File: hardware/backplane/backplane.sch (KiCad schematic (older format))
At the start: 12 parts, among them J1 C96ABC, J2 C96ABC, J3 C96ABC, J4 C96ABC, J5 C96ABC, J6 C96ABC, J7 C96ABC, J8 C96ABC

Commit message: start to put clock hardware on the backplane
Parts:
- added C1, C2: 0.01μF, Capacitor_THT:C_Rect_L7.0mm_W3.5mm_P5.00mm, symbol Device:C
- added C3, C4: 1μF, Capacitor_THT:C_Rect_L7.0mm_W3.5mm_P5.00mm, symbol Device:C
- added CB1, CB2, CB3, CB4, CB5, CB6: 0.1μF, Capacitor_THT:C_Rect_L7.0mm_W3.5mm_P5.00mm, symbol Device:C_Small
- added CBU1, CBU2, CBU3, CBU4, CBX1: 0.1μF, Capacitor_THT:C_Rect_L7.0mm_W3.5mm_P5.00mm, symbol Device:C
- added CR1, CR2: 1μF, Capacitor_THT:C_Rect_L7.0mm_W3.5mm_P5.00mm, symbol Device:C_Small
- added D1, D2: DIODE, Diode_THT:D_DO-15_P2.54mm_Vertical_AnodeUp, symbol pspice:DIODE
- added J9: C96ABC, Connector_DIN:DIN41612_C_3x32_Female_Vertical_THT, symbol Connector:C96ABC
- added JP1: Jumper_NO_Small, Connector_PinHeader_2.54mm:PinHeader_1x02_P2.54mm_Vertical, symbol Device:Jumper_NO_Small
- added JPC1: JP_RST, Connector_PinHeader_2.54mm:PinHeader_1x02_P2.54mm_Vertical, symbol Jumper:Jumper_2_Open
- added R1, R9: 4.7k, Resistor_THT:R_Axial_DIN0207_L6.3mm_D2.5mm_P2.54mm_Vertical, symbol Device:R
- added R10, R11, R4, R6, R7, R8: 1k, Resistor_THT:R_Axial_DIN0207_L6.3mm_D2.5mm_P2.54mm_Vertical, symbol Device:R
- added R2: 1M, Resistor_THT:R_Axial_DIN0207_L6.3mm_D2.5mm_P2.54mm_Vertical, symbol Device:R
- added R3: 100k, Resistor_THT:R_Axial_DIN0207_L6.3mm_D2.5mm_P2.54mm_Vertical, symbol Device:R
- added R5: 100k, Connector_PinHeader_2.54mm:PinHeader_1x02_P2.54mm_Vertical, symbol Device:R_Variable
- added SW1: SW_Push, Connector_PinHeader_2.54mm:PinHeader_1x02_P2.54mm_Vertical, symbol Switch:SW_Push
- added SW2, SW3: SW_SPDT, Connector_PinHeader_2.54mm:PinHeader_1x03_P2.54mm_Vertical, symbol Switch:SW_SPDT
- added U1: 74AHC14, Package_DIP:DIP-14_W7.62mm_Socket, symbol 74xx:74LS14
- added U10: U13, Package_DIP:DIP-14_W7.62mm_Socket, symbol 74xx:74HC00
- added U2, U3: 74AHC08, Package_DIP:DIP-14_W7.62mm_Socket, symbol 74xx:74LS08
- added U4: 74HC00, Package_DIP:DIP-14_W7.62mm_Socket, symbol 74xx:74HC00
- added U5, U6: 74AHC74, Package_DIP:DIP-14_W7.62mm_Socket, symbol 74xx:74LS74
- added U7: NE556, Package_DIP:DIP-14_W7.62mm_Socket, symbol Timer:NE556
- added U8: 74AHC32, Package_DIP:DIP-14_W7.62mm_Socket, symbol 74xx:74LS32
- added U9: 74AHCT125, Package_DIP:DIP-14_W7.62mm_Socket, symbol 74xx:74LS125
- added X1: CXO_DIP8, Package_DIP:DIP-8_W7.62mm_Socket, symbol Oscillator:CXO_DIP8
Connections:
- net A10: now also J9.A10 (10A)
- net A11: now also J9.A11 (11A)
- net A12: now also J9.A12 (12A)
- net A13: now also J9.A13 (13A)
- net A14: now also J9.A14 (14A)
- net A15: now also J9.A15 (15A)
- net A16: now also J9.A16 (16A)
- net A17: now also J9.A17 (17A)
- net A18: now also J9.A18 (18A)
- net A19: now also J9.A19 (19A)
- net A2: now also J9.A2 (2A)
- net A20: now also J9.A20 (20A)
- net A21: now also J9.A21 (21A)
- net A22: now also J9.A22 (22A)
- net A23: now also J9.A23 (23A)
- net A24: now also J9.A24 (24A)
- net A25: now also J9.A25 (25A)
- net A26: now also J9.A26 (26A)
- net A27: now also J9.A27 (27A), U2.4
- net A28: now also J9.A28 (28A), U8.8
- net A29: now also J9.A29 (29A)
- net A3: now also J9.A3 (3A)
- net A30: now also J9.A30 (30A)
- net A31: now also J9.A31 (31A), U1.1, U2.9, U6.11 (C)
- net A4: now also J9.A4 (4A)
- net A5: now also J9.A5 (5A)
- net A6: now also J9.A6 (6A)
- net A7: now also J9.A7 (7A)
- net A8: now also J9.A8 (8A)
- net A9: now also J9.A9 (9A)
- net C10: now also J9.C10 (10C)
- net C11: now also J9.C11 (11C)
- net C12: now also J9.C12 (12C)
- net C13: now also J9.C13 (13C)
- net C14: now also J9.C14 (14C)
- net C15: now also J9.C15 (15C)
- net C16: now also J9.C16 (16C)
- net C17: now also J9.C17 (17C)
- net C18: now also J9.C18 (18C)
- net C19: now also J9.C19 (19C)
- net C2: now also J9.C2 (2C)
- net C20: now also J9.C20 (20C)
- net C21: now also J9.C21 (21C)
- net C22: now also J9.C22 (22C)
- net C23: now also J9.C23 (23C), U1.8
- net C24: now also J9.C24 (24C)
- net C25: now also J9.C25 (25C)
- net C26: now also J9.C26 (26C)
- net C27: now also J9.C27 (27C)
- net C28: now also J9.C28 (28C)
- net C29: now also J9.C29 (29C)
- net C3: now also J9.C3 (3C)
- net C30: now also J9.C30 (30C)
- net C31: now also D1.2 (A), D2.2 (A), J9.C31 (31C), JPC1.1 (A), R1.2
- net C4: now also J9.C4 (4C)
- net C5: now also J9.C5 (5C)
- net C6: now also J9.C6 (6C)
- net C7: now also J9.C7 (7C)
- net C8: now also J9.C8 (8C)
- net C9: now also J9.C9 (9C)
- net GND: now also C1.2, C2.2, C3.2, C4.2, CB1.2, CB2.2, CB3.2, CB4.2, CB5.2, CB6.1, CBU1.2, CBU2.2, CBU3.2, CBU4.2, CBX1.2, CR1.2, CR2.2, J9.A32 (32A), J9.B32 (32B), J9.C32 (32C), JP1.1, JPC1.2 (B), SW1.1, SW3.2 (B), U1.7 (GND), U10.7 (GND), U2.7 (GND), U3.10, U3.12, U3.13, U3.4, U3.5, U3.7 (GND), U3.9, U4.7 (GND), U5.7 (GND), U6.7 (GND), U7.7 (GND), U7.7 (GND), U8.7 (GND), U9.7 (GND), X1.4 (GND)
- net VCC: now also CB1.1, CB2.1, CB3.1, CB4.1, CB5.1, CB6.2, CBU1.1, CBU2.1, CBU3.1, CBU4.1, CBX1.1, J9.A1 (1A), J9.B1 (1B), J9.C1 (1C), R1.1, R10.1, R11.1, R2.1, R3.1, R4.1, R7.1, R8.1, R9.1, U1.14 (VCC), U10.14 (VCC), U2.14 (VCC), U3.14 (VCC), U4.14 (VCC), U5.14 (VCC), U6.14 (VCC), U7.10 (R), U7.14 (VCC), U7.14 (VCC), U7.4 (R), U8.14 (VCC), U9.14 (VCC), X1.8 (Vcc)
- new net: U1.2, U5.3 (C)
- new net: U1.4, U6.3 (C)
- new net: U1.11, U1.12
- new net: U2.11, U8.10
- new net: U2.8, U8.9
- new net: U3.1, U9.11
- new net: SW2.2 (B), U9.12
- new net: U2.3, U5.2 (D)
- new net: U5.5 (Q), U6.12 (D)
- new net: U2.6, U6.2 (D)
- new net: U5.12 (D), U6.5 (Q)
- new net: U2.2, U5.8 (~Q)
- new net: U2.12, U5.9 (Q)
- new net: U2.5, U6.8 (~Q)
- new net: U2.10, U6.9 (Q)
- new net: CR1.1, D1.1 (K), R2.2, U1.5
- new net: R5.1, R6.1
- new net: R6.2, R7.2, U7.1 (DIS)
- new net: C3.1, R5.2, U7.2 (THR), U7.6 (TR)
- new net: C1.1, U7.3 (CV)
- new net: CR2.1, D2.1 (K), R3.2, U1.13
- new net: C4.1, R8.2, U7.12 (THR), U7.13 (DIS)
- new net: R4.2, SW1.2, U7.8 (TR)
- new net: C2.1, U7.11 (CV)
- new net: R11.2, SW3.1 (A), U10.1
- new net: R10.2, SW3.3 (C), U10.5
- new net: U4.10, U4.6
- new net: U4.3, U4.9
- new net +5V: U5.10 (~S), U5.4 (~S), U6.10 (~S), U6.4 (~S)
- new net 555_AST: U4.2, U7.5 (Q)
- new net 555_CLK: SW2.3 (C), U4.8
- new net 555_MONO: U4.5, U7.9 (Q)
- new net BASE_CLK: U3.3
- new net BUS_ACTIVE: U2.1
- new net RST-unused: U1.6, U1.9
- new net SEL_AST: U10.3, U10.4, U4.1
- new net SEL_MONO: U10.2, U10.6, U4.4
- new net SYS_CLK: U1.3, U2.13, U5.11 (C)
- new net XO: SW2.1 (A), X1.5 (OUT)
- new net ~CLK_ENABLE~: JP1.2, R9.2, U9.13
- new net ~CLK_RST~: U1.10, U3.2, U5.1 (~R), U5.13 (~R), U6.1 (~R), U6.13 (~R)
- no-connect marks 30 -> 66
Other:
- note added: "Clock switcher"
- note added: "Reset signals"
- note added: "shorter clock rst pulse s.t. \nclock starts before other ICs"
- moved on the sheet: H1, H2, H3, H4, J1, J2, J3, J4, J5, J6, J7, J8

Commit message: backplane: shrink by 1mm in both dimensions and start rearranging components
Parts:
- H4: footprint rails:SHF8-R -> rails:SHF8-L
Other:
- moved on the sheet: H1, H2, H3, H4
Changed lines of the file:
@@
 L Mechanical:MountingHole H4
 U 1 1 6046743B
-P -850 -7950
-F 0 "H4" H -750 -7904 50  0000 L CNN
-F 1 "MountingHole" H -750 -7995 50  0000 L CNN
-F 2 "rails:SHF8-R" H -850 -7950 50  0001 C CNN
-F 3 "~" H -850 -7950 50  0001 C CNN
-	1    -850 -7950
+P -2500 8100
+F 0 "H4" H -2400 8146 50  0000 L CNN
+F 1 "MountingHole" H -2400 8055 50  0000 L CNN
+F 2 "rails:SHF8-L" H -2500 8100 50  0001 C CNN
+F 3 "~" H -2500 8100 50  0001 C CNN
+	1    -2500 8100
 	1    0    0    -1
 $EndComp
@@
 L Mechanical:MountingHole H3
 U 1 1 604683EA
-P -950 -8550
-F 0 "H3" H -850 -8504 50  0000 L CNN
-F 1 "MountingHole" H -850 -8595 50  0000 L CNN
-F 2 "rails:SHF8-L" H -950 -8550 50  0001 C CNN
-F 3 "~" H -950 -8550 50  0001 C CNN
-	1    -950 -8550
+P -2600 7500
+F 0 "H3" H -2500 7546 50  0000 L CNN
+F 1 "MountingHole" H -2500 7455 50  0000 L CNN
+F 2 "rails:SHF8-L" H -2600 7500 50  0001 C CNN
+F 3 "~" H -2600 7500 50  0001 C CNN
+	1    -2600 7500
 	1    0    0    -1
 $EndComp
@@
 L Mechanical:MountingHole H2
 U 1 1 60468515
-P -1050 -9000
-F 0 "H2" H -950 -8954 50  0000 L CNN
-F 1 "MountingHole" H -950 -9045 50  0000 L CNN
-F 2 "rails:SHF8-R" H -1050 -9000 50  0001 C CNN
-F 3 "~" H -1050 -9000 50  0001 C CNN
-	1    -1050 -9000
+P -2700 7050
+F 0 "H2" H -2600 7096 50  0000 L CNN
+F 1 "MountingHole" H -2600 7005 50  0000 L CNN
+F 2 "rails:SHF8-R" H -2700 7050 50  0001 C CNN
+F 3 "~" H -2700 7050 50  0001 C CNN
+	1    -2700 7050
 	1    0    0    -1
 $EndComp
@@
 L Mechanical:MountingHole H1
 U 1 1 604686C3
-P -1050 -9550
-F 0 "H1" H -950 -9504 50  0000 L CNN
-F 1 "MountingHole" H -950 -9595 50  0000 L CNN
-F 2 "rails:SHF8-L" H -1050 -9550 50  0001 C CNN
-F 3 "~" H -1050 -9550 50  0001 C CNN
-	1    -1050 -9550
+P -2700 6500
+F 0 "H1" H -2600 6546 50  0000 L CNN
+F 1 "MountingHole" H -2600 6455 50  0000 L CNN
+F 2 "rails:SHF8-L" H -2700 6500 50  0001 C CNN
+F 3 "~" H -2700 6500 50  0001 C CNN
+	1    -2700 6500
 	1    0    0    -1
 $EndComp

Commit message: backplane: remove the base/bus clock switch
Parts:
- removed CB1, CB3, CB4, CB5, CB6: 0.1μF, Capacitor_THT:C_Rect_L7.0mm_W3.5mm_P5.00mm, symbol Device:C_Small
- removed U3: 74AHC08, Package_DIP:DIP-14_W7.62mm_Socket, symbol 74xx:74LS08
- removed U5, U6: 74AHC74, Package_DIP:DIP-14_W7.62mm_Socket, symbol 74xx:74LS74
- removed U8: 74AHC32, Package_DIP:DIP-14_W7.62mm_Socket, symbol 74xx:74LS32
- added J10: Conn_Coaxial_Power, Connector_Phoenix_MSTB:PhoenixContact_MSTBVA_2,5_2-G-5,08_1x02_P5.08mm_Vertical, symbol Connector:Conn_Coaxial_Power
- added TP1, TP10, TP11, TP12, TP13, TP14, TP15, TP16, TP17, TP18, TP19, TP2, TP20, TP21, TP22, TP23, TP24, TP25, TP26, TP27, TP28, TP29, TP3, TP30, TP4, TP5, TP6, TP7, TP8, TP9: TestPoint, TestPoint:TestPoint_THTPad_D1.0mm_Drill0.5mm, symbol Connector:TestPoint
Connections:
- net BUS_ACTIVE is gone; now on net GND: U2.1
- net A27: no longer U2.4
- net A28: now also U2.11
- net A31: no longer U1.1, U2.9
- net B10J1: now also TP9.1
- net B11J1: now also TP10.1
- net B12J1: now also TP11.1
- net B13J1: now also TP12.1
- net B14J1: now also TP13.1
- net B15J1: now also TP14.1
- net B16J1: now also TP15.1
- net B17J1: now also TP16.1
- net B18J1: now also TP17.1
- net B19J1: now also TP18.1
- net B20J1: now also TP19.1
- net B21J1: now also TP20.1
- net B22J1: now also TP21.1
- net B23J1: now also TP22.1
- net B24J1: now also TP23.1
- net B25J1: now also TP24.1
- net B26J1: now also TP25.1
- net B27J1: now also TP26.1
- net B28J1: now also TP27.1
- net B29J1: now also TP28.1
- net B2J1: now also TP1.1
- net B30J1: now also TP29.1
- net B31J1: now also TP30.1
- net B3J1: now also TP2.1
- net B4J1: now also TP3.1
- net B5J1: now also TP4.1
- net B6J1: now also TP5.1
- net B7J1: now also TP6.1
- net B8J1: now also TP7.1
- net B9J1: now also TP8.1
- net C31: no longer D1.2 (A), D2.2 (A), JPC1.1 (A), R1.2
- net GND: now also U1.1, U1.3, U10.10, U10.12, U10.13, U10.9, U2.10, U2.2, U2.4, U2.5, U2.9, U4.12, U4.13, U9.2, U9.5, U9.9, J10.2 (Ext)
- net VCC: now also U9.1, U9.10, U9.4, J10.1 (In)
- net ~CLK_RST~: now also U2.13
- net CLK_RST: now reaches U1.11, U1.12
- net at U9.11: now also U2.12
- net RST-unused: no longer names the net of U1.6, U1.9
- removed net SYS_CLK: U1.3, U2.13
- new net ~RST_HDR~: D1.2 (A), D2.2 (A), JPC1.1 (A), R1.2
- no-connect marks 66 -> 72
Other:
- note removed: "Clock switcher"
- moved on the sheet: C1, C2, C3, C4, CB2, CBU1, CBU2, CBU3, CBU4, CBX1, CR1, CR2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

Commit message: backplane: bump some clearance hole diameters
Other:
- moved on the sheet: C1, C2, C3, C4, CR1, CR2, D1, D2, H1, H2, H3, H4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

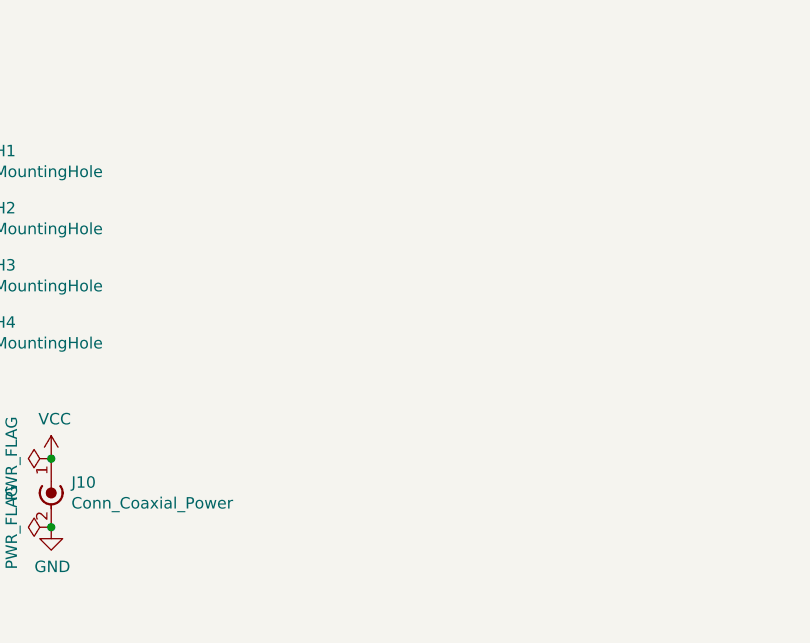
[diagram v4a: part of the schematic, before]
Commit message: backplane: use less mounting hardware
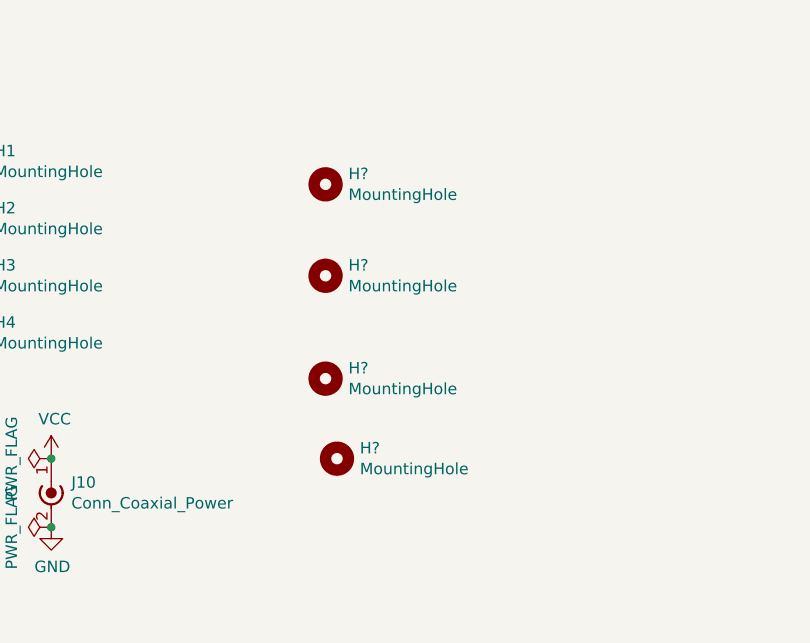
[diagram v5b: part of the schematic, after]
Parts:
- added H? (x4): MountingHole, rails:7mm, symbol Mechanical:MountingHole
- H1, H3, H4: footprint rails:SHF8-L -> rails:8mm
- H2: footprint rails:SHF8-R -> rails:8mm
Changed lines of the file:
@@
 F 0 "H4" H 12250 5546 50  0000 L CNN
 F 1 "MountingHole" H 12250 5455 50  0000 L CNN
-F 2 "rails:SHF8-L" H 12150 5500 50  0001 C CNN
+F 2 "rails:8mm" H 12150 5500 50  0001 C CNN
 F 3 "~" H 12150 5500 50  0001 C CNN
 	1    12150 5500
@@
 F 0 "H3" H 12250 5296 50  0000 L CNN
 F 1 "MountingHole" H 12250 5205 50  0000 L CNN
-F 2 "rails:SHF8-L" H 12150 5250 50  0001 C CNN
+F 2 "rails:8mm" H 12150 5250 50  0001 C CNN
 F 3 "~" H 12150 5250 50  0001 C CNN
 	1    12150 5250
@@
 F 0 "H2" H 12250 5046 50  0000 L CNN
 F 1 "MountingHole" H 12250 4955 50  0000 L CNN
-F 2 "rails:SHF8-R" H 12150 5000 50  0001 C CNN
+F 2 "rails:8mm" H 12150 5000 50  0001 C CNN
 F 3 "~" H 12150 5000 50  0001 C CNN
 	1    12150 5000
@@
 F 0 "H1" H 12250 4796 50  0000 L CNN
 F 1 "MountingHole" H 12250 4705 50  0000 L CNN
-F 2 "rails:SHF8-L" H 12150 4750 50  0001 C CNN
+F 2 "rails:8mm" H 12150 4750 50  0001 C CNN
 F 3 "~" H 12150 4750 50  0001 C CNN
 	1    12150 4750
@@
 Wire Wire Line
 	-650 -2650 -700 -2650
+$Comp
+L Mechanical:MountingHole H?
+U 1 1 A242A775
+P 13700 4850
+F 0 "H?" H 13800 4896 50  0000 L CNN
+F 1 "MountingHole" H 13800 4805 50  0000 L CNN
+F 2 "rails:7mm" H 13700 4850 50  0001 C CNN
+F 3 "~" H 13700 4850 50  0001 C CNN
+	1    13700 4850
+	1    0    0    -1
+$EndComp
+$Comp
+L Mechanical:MountingHole H?
+U 1 1 A2589AFB
+P 13700 5250
+F 0 "H?" H 13800 5296 50  0000 L CNN
+F 1 "MountingHole" H 13800 5205 50  0000 L CNN
+F 2 "rails:7mm" H 13700 5250 50  0001 C CNN
+F 3 "~" H 13700 5250 50  0001 C CNN
+	1    13700 5250
+	1    0    0    -1
+$EndComp
+$Comp
+L Mechanical:MountingHole H?
+U 1 1 A2589DC3
+P 13700 5700
+F 0 "H?" H 13800 5746 50  0000 L CNN
+F 1 "MountingHole" H 13800 5655 50  0000 L CNN
+F 2 "rails:7mm" H 13700 5700 50  0001 C CNN
+F 3 "~" H 13700 5700 50  0001 C CNN
+	1    13700 5700
+	1    0    0    -1
+$EndComp
+$Comp
+L Mechanical:MountingHole H?
+U 1 1 A2589F42
+P 13750 6050
+F 0 "H?" H 13850 6096 50  0000 L CNN
+F 1 "MountingHole" H 13850 6005 50  0000 L CNN
+F 2 "rails:7mm" H 13750 6050 50  0001 C CNN
+F 3 "~" H 13750 6050 50  0001 C CNN
+	1    13750 6050
+	1    0    0    -1
+$EndComp
 $EndSCHEMATC
